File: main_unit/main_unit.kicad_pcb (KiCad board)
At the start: 2 copper layers, 90 x 65 mm, 93 parts, among them J1 PROG_UART_3V3, J2 DM3CS-SF, J3 OLED_SH1106_I2C, J4 PACK_2S_P+/P-, J5 GPS_UART_3V3, SW1 RESET, SW2 BOOT, SW3 START_STOP, SW4 POWER_ON_OFF, U1 ESP32-WROOM-32E-N4, U2 ADXL345BCCZ-RL7, U3 DS3231SN#, U4 MP1584 MODULE 3V3 (PROV)

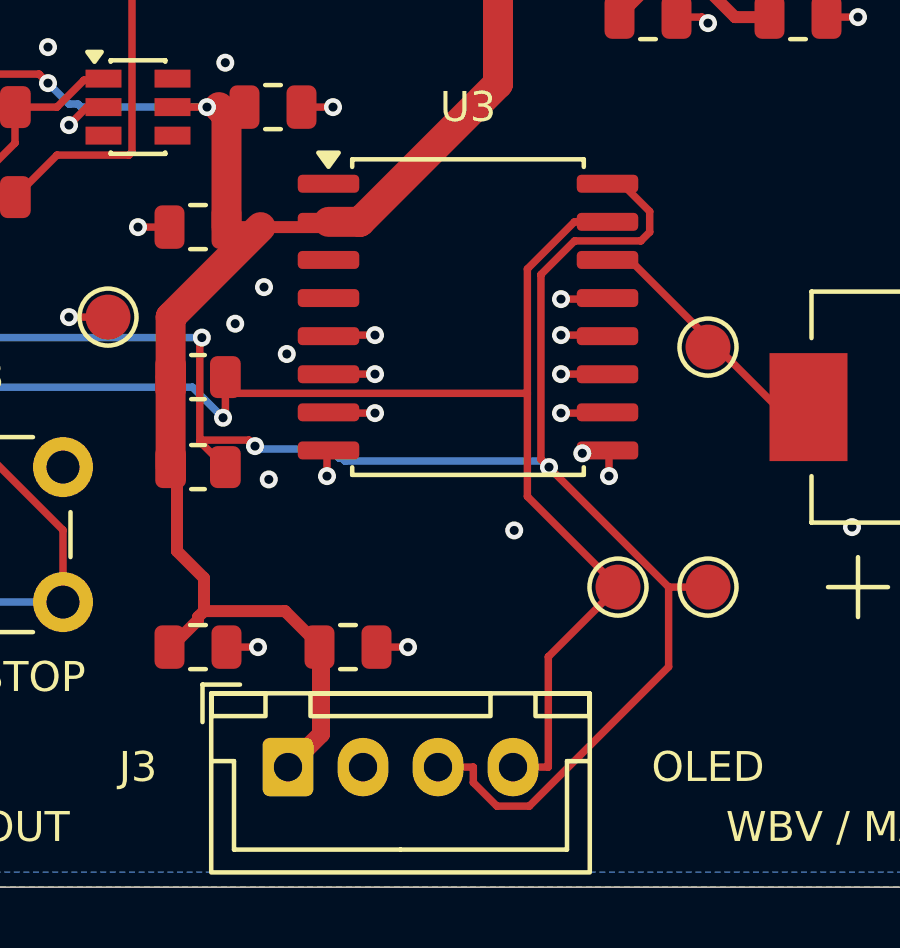
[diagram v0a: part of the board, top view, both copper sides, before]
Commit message: Fix WBV RTC I2C routing and publish JLCPCB R2 package
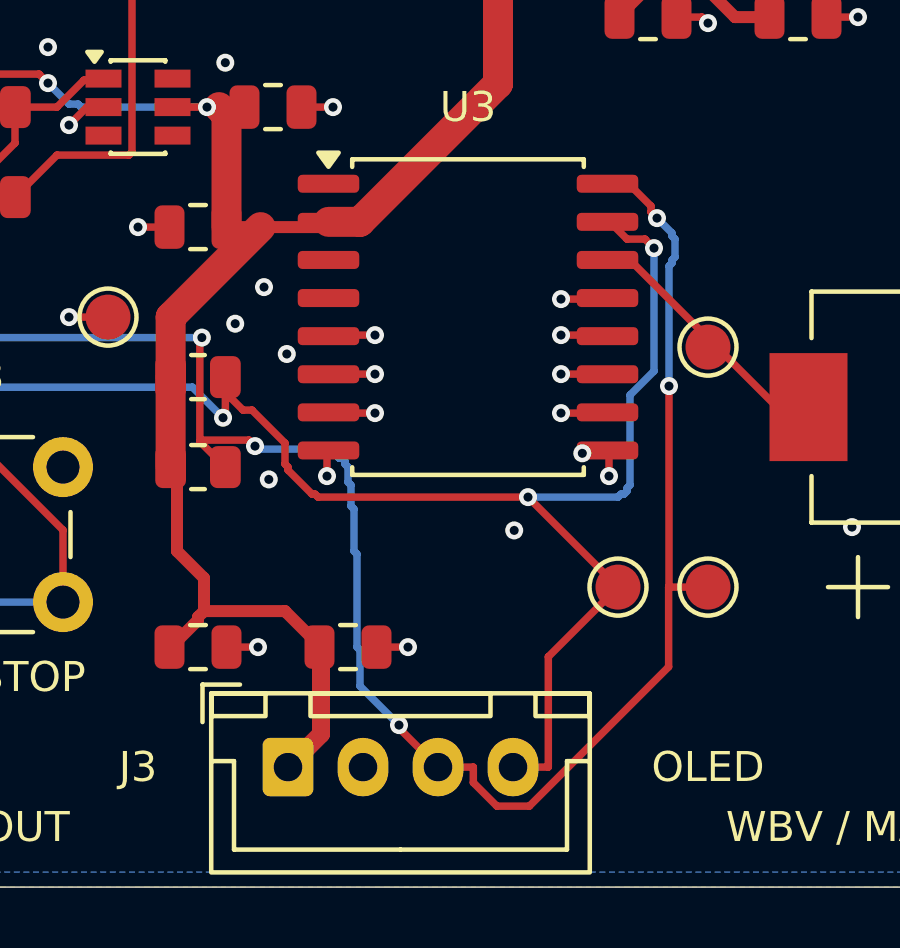
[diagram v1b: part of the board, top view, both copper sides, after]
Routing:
- net I2C_SDA: track 113.3 -> 118.3 mm, vias 2 -> 4
- net I2C_SCL: track 133.8 -> 134.4 mm, vias 6 -> 8
